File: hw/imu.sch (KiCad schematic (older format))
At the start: 1 part

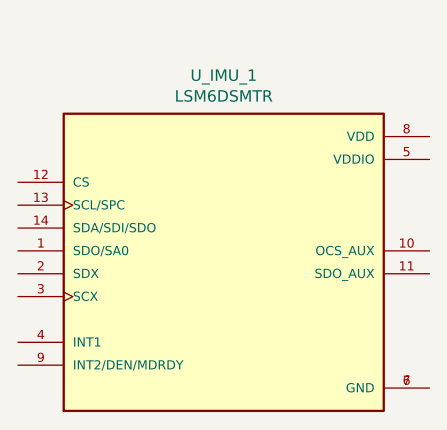
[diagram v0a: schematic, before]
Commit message: add esp32 and IMU components to schematics
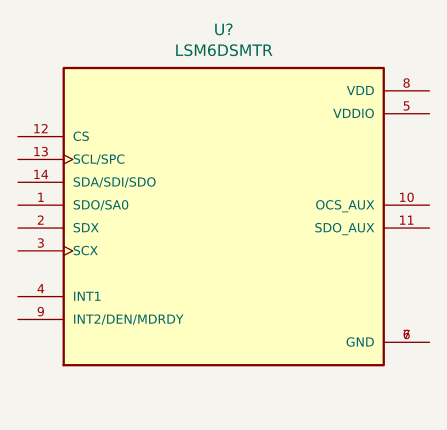
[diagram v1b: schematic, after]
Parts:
- removed U_IMU_1: LSM6DSMTR, PQFN50P300X250X86-14N, symbol LSM6DSMTR:LSM6DSMTR
- added U?: LSM6DSMTR, PQFN50P300X250X86-14N, symbol LSM6DSMTR:LSM6DSMTR
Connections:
- new net: U?.6 (GND), U?.7 (GND)
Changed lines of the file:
@@
 $EndDescr
 $Comp
-L LSM6DSMTR:LSM6DSMTR U_IMU_1
-U 1 1 609A00F1
-P 5550 3600
-F 0 "U_IMU_1" H 5550 4367 50  0000 C CNN
-F 1 "LSM6DSMTR" H 5550 4276 50  0000 C CNN
-F 2 "PQFN50P300X250X86-14N" H 5550 3600 50  0001 L BNN
-F 3 "" H 5550 3600 50  0001 L BNN
-F 4 "Rev 7" H 5550 3600 50  0001 L BNN "PARTREV"
-F 5 "STMicroelectronics" H 5550 3600 50  0001 L BNN "MANUFACTURER"
-F 6 "0.86 mm" H 5550 3600 50  0001 L BNN "MAXIMUM_PACKAGE_HEIGHT"
-F 7 "IPC 7351B" H 5550 3600 50  0001 L BNN "STANDARD"
-	1    5550 3600
+L LSM6DSMTR:LSM6DSMTR U?
+U 1 1 609A2074
+P 5550 3400
+F 0 "U?" H 5550 4167 50  0000 C CNN
+F 1 "LSM6DSMTR" H 5550 4076 50  0000 C CNN
+F 2 "PQFN50P300X250X86-14N" H 5550 3400 50  0001 L BNN
+F 3 "" H 5550 3400 50  0001 L BNN
+F 4 "Rev 7" H 5550 3400 50  0001 L BNN "PARTREV"
+F 5 "STMicroelectronics" H 5550 3400 50  0001 L BNN "MANUFACTURER"
+F 6 "0.86 mm" H 5550 3400 50  0001 L BNN "MAXIMUM_PACKAGE_HEIGHT"
+F 7 "IPC 7351B" H 5550 3400 50  0001 L BNN "STANDARD"
+	1    5550 3400
 	1    0    0    -1
 $EndComp

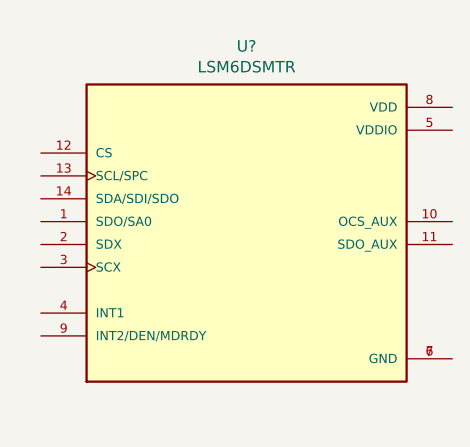
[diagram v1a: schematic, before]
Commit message: Modified ESP32 and IMU symbol properties. Generated netlist and tables as example
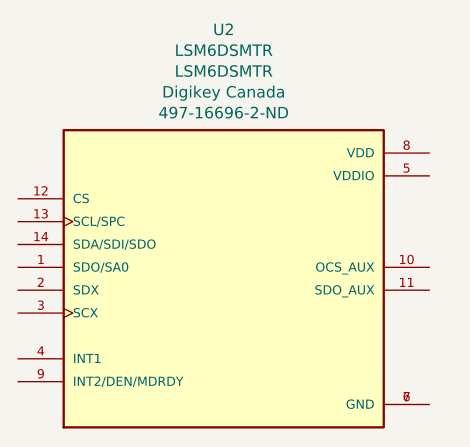
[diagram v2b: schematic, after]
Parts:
- removed U?: LSM6DSMTR, PQFN50P300X250X86-14N, symbol LSM6DSMTR:LSM6DSMTR
- added U2: LSM6DSMTR, footprints:LSM6DSMTR, symbol LSM6DSMTR:LSM6DSMTR
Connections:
- new net: U2.6 (GND), U2.7 (GND)
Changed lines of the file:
@@
 $EndDescr
 $Comp
-L LSM6DSMTR:LSM6DSMTR U?
-U 1 1 609A2074
-P 5550 3400
-F 0 "U?" H 5550 4167 50  0000 C CNN
-F 1 "LSM6DSMTR" H 5550 4076 50  0000 C CNN
-F 2 "PQFN50P300X250X86-14N" H 5550 3400 50  0001 L BNN
-F 3 "" H 5550 3400 50  0001 L BNN
-F 4 "Rev 7" H 5550 3400 50  0001 L BNN "PARTREV"
-F 5 "STMicroelectronics" H 5550 3400 50  0001 L BNN "MANUFACTURER"
-F 6 "0.86 mm" H 5550 3400 50  0001 L BNN "MAXIMUM_PACKAGE_HEIGHT"
-F 7 "IPC 7351B" H 5550 3400 50  0001 L BNN "STANDARD"
-	1    5550 3400
+L LSM6DSMTR:LSM6DSMTR U2
+U 1 1 609A33A3
+P 5450 3600
+F 0 "U2" H 5450 4639 50  0000 C CNN
+F 1 "LSM6DSMTR" H 5450 4548 50  0000 C CNN
+F 2 "footprints:LSM6DSMTR" H 5450 3600 50  0001 L BNN
+F 3 "http://www.st.com/content/ccc/resource/technical/document/datasheet/76/27/cf/88/c5/03/42/6b/DM00218116.pdf/files/DM00218116.pdf/jcr:content/translations/en.DM00218116.pdf" H 5450 3600 50  0001 L BNN
+F 4 "Rev 7" H 5450 3600 50  0001 L BNN "PARTREV"
+F 5 "0.86 mm" H 5450 3600 50  0001 L BNN "MAXIMUM_PACKAGE_HEIGHT"
+F 6 "IPC 7351B" H 5450 3600 50  0001 L BNN "STANDARD"
+F 7 "STMicroelectronics" H 5450 3600 50  0001 L BNN "Manufacturer"
+F 8 "LSM6DSMTR" H 5450 4457 50  0000 C CNN "Manufacturer Product Number"
+F 9 "Digikey Canada" H 5450 4366 50  0000 C CNN "Vendor"
+F 10 "497-16696-2-ND" H 5450 4275 50  0000 C CNN "Vendor Product Number"
+	1    5450 3600
 	1    0    0    -1
 $EndComp

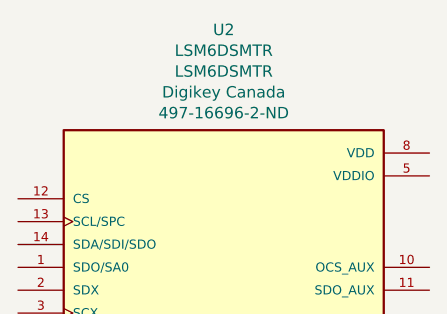
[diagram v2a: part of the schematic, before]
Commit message: Updated schematics and footprints to use default shared libraries. Updated general schematic
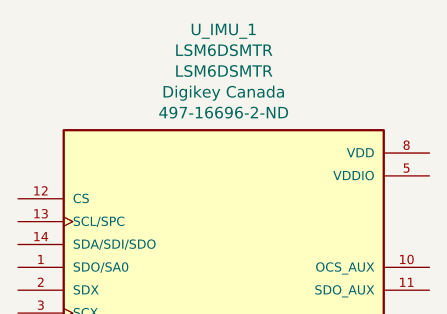
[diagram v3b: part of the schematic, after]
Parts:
- U_IMU_1: renamed from U2; MAXIMUM_PACKAGE_HEIGHT 0.86 mm -> (none); PARTREV Rev 7 -> (none); STANDARD IPC 7351B -> (none)
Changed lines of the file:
@@
 $EndDescr
 $Comp
-L LSM6DSMTR:LSM6DSMTR U2
+L LSM6DSMTR:LSM6DSMTR U_IMU_1
 U 1 1 609A33A3
 P 5450 3600
-F 0 "U2" H 5450 4639 50  0000 C CNN
+F 0 "U_IMU_1" H 5450 4639 50  0000 C CNN
 F 1 "LSM6DSMTR" H 5450 4548 50  0000 C CNN
 F 2 "footprints:LSM6DSMTR" H 5450 3600 50  0001 L BNN
 F 3 "http://www.st.com/content/ccc/resource/technical/document/datasheet/76/27/cf/88/c5/03/42/6b/DM00218116.pdf/files/DM00218116.pdf/jcr:content/translations/en.DM00218116.pdf" H 5450 3600 50  0001 L BNN
-F 4 "Rev 7" H 5450 3600 50  0001 L BNN "PARTREV"
-F 5 "0.86 mm" H 5450 3600 50  0001 L BNN "MAXIMUM_PACKAGE_HEIGHT"
-F 6 "IPC 7351B" H 5450 3600 50  0001 L BNN "STANDARD"
-F 7 "STMicroelectronics" H 5450 3600 50  0001 L BNN "Manufacturer"
-F 8 "LSM6DSMTR" H 5450 4457 50  0000 C CNN "Manufacturer Product Number"
-F 9 "Digikey Canada" H 5450 4366 50  0000 C CNN "Vendor"
-F 10 "497-16696-2-ND" H 5450 4275 50  0000 C CNN "Vendor Product Number"
+F 4 "STMicroelectronics" H 5450 3600 50  0001 L BNN "Manufacturer"
+F 5 "LSM6DSMTR" H 5450 4457 50  0000 C CNN "Manufacturer Product Number"
+F 6 "Digikey Canada" H 5450 4366 50  0000 C CNN "Vendor"
+F 7 "497-16696-2-ND" H 5450 4275 50  0000 C CNN "Vendor Product Number"
 	1    5450 3600
 	1    0    0    -1

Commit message: minor changes
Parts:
- added IMU_C1: 0.1uF, footprints:C1206S104K5RACAUTO, symbol Device:C_Small
- added IMU_R1, IMU_R2: 4.7k, footprints:RESC1508X55N, symbol Device:R
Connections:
- net labels added: +3.3V, +3.3V_cap, GND, IMU_INT1, IMU_INT2, IMU_SCL, IMU_SDA, IMU_SDO_SA0
- wire segments 0 -> 28
- no-connect marks 0 -> 2
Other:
- moved on the sheet: U_IMU_1
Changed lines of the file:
@@
 $EndDescr
+$Comp
+L power:+3.3V #PWR?
+U 1 1 60AD089D
+P 1550 1200
+F 0 "#PWR?" H 1550 1050 50  0001 C CNN
+F 1 "+3.3V" H 1565 1373 50  0000 C CNN
+F 2 "" H 1550 1200 50  0001 C CNN
+F 3 "" H 1550 1200 50  0001 C CNN
+	1    1550 1200
+	1    0    0    -1
+$EndComp
+$Comp
+L power:+3.3V #PWR?
+U 1 1 60ACF823
+P 3450 2400
+F 0 "#PWR?" H 3450 2250 50  0001 C CNN
+F 1 "+3.3V" H 3465 2573 50  0000 C CNN
+F 2 "" H 3450 2400 50  0001 C CNN
+F 3 "" H 3450 2400 50  0001 C CNN
+	1    3450 2400
+	1    0    0    -1
+$EndComp
+Wire Wire Line
+	4150 3700 4150 4200
+$Comp
+L power:GND #PWR?
+U 1 1 60ACE4E5
+P 6600 4350
+F 0 "#PWR?" H 6600 4100 50  0001 C CNN
+F 1 "GND" H 6605 4177 50  0000 C CNN
+F 2 "" H 6600 4350 50  0001 C CNN
+F 3 "" H 6600 4350 50  0001 C CNN
+	1    6600 4350
+	1    0    0    -1
+$EndComp
+$Comp
+L power:GND #PWR?
+U 1 1 60ACD629
+P 4150 4200
+F 0 "#PWR?" H 4150 3950 50  0001 C CNN
+F 1 "GND" H 4155 4027 50  0000 C CNN
+F 2 "" H 4150 4200 50  0001 C CNN
+F 3 "" H 4150 4200 50  0001 C CNN
+	1    4150 4200
+	1    0    0    -1
+$EndComp
+$Comp
+L power:GND #PWR?
+U 1 1 60ACC949
+P 1550 2000
+F 0 "#PWR?" H 1550 1750 50  0001 C CNN
+F 1 "GND" H 1555 1827 50  0000 C CNN
+F 2 "" H 1550 2000 50  0001 C CNN
+F 3 "" H 1550 2000 50  0001 C CNN
+	1    1550 2000
+	1    0    0    -1
+$EndComp
+Wire Wire Line
+	1550 1750 1550 2000
+Connection ~ 3450 2700
+Wire Wire Line
+	3450 2400 3450 2700
+Wire Wire Line
+	3450 2700 3450 2800
+Wire Wire Line
+	3950 2700 3450 2700
+Wire Wire Line
+	3950 2800 3950 2700
+Wire Wire Line
+	2400 3300 3950 3300
+Wire Wire Line
+	3950 3300 4650 3300
+Connection ~ 3950 3300
+Wire Wire Line
+	4200 3200 4650 3200
+Text Label 4200 3200 0    50   ~ 0
++3.3V_cap
+$Comp
+L Device:R IMU_R2
+U 1 1 60A2D06B
+P 3950 2950
+F 0 "IMU_R2" H 4020 2996 50  0000 L CNN
+F 1 "4.7k" H 4020 2905 50  0000 L CNN
+F 2 "footprints:RESC1508X55N" V 3880 2950 50  0001 C CNN
+F 3 "~https://www.vishay.com/docs/28760/mcat_pro.pdf" H 3950 2950 50  0001 C CNN
+F 4 "Digikey" H 3950 2950 50  0001 C CNN "Vendor"
+F 5 "MCT0603-4.7K-MDCT-ND" H 3950 2950 50  0001 C CNN "Vendor Part Number"
+F 6 "Vishay Beyschlag/Draloric/BC Components" H 3950 2950 50  0001 C CNN "Manufacturer"
+F 7 "MCT0603MD4701DP500" H 3950 2950 50  0001 C CNN "Manufacturer Part Number"
+	1    3950 2950
+	1    0    0    -1
+$EndComp
+Wire Wire Line
+	6600 4100 6600 4350
+Wire Wire Line
+	6450 4100 6600 4100
+Wire Wire Line
+	3950 3100 3950 3300
+Wire Wire Line
+	3450 3400 4650 3400
+Connection ~ 3450 3400
+Wire Wire Line
+	3450 3100 3450 3400
+$Comp
+L Device:R IMU_R1
+U 1 1 60A29787
+P 3450 2950
+F 0 "IMU_R1" H 3520 2996 50  0000 L CNN
+F 1 "4.7k" H 3520 2905 50  0000 L CNN
+F 2 "footprints:RESC1508X55N" V 3380 2950 50  0001 C CNN
+F 3 "~https://www.vishay.com/docs/28760/mcat_pro.pdf" H 3450 2950 50  0001 C CNN
+F 4 "Digikey" H 3450 2950 50  0001 C CNN "Vendor"
+F 5 "MCT0603-4.7K-MDCT-ND" H 3450 2950 50  0001 C CNN "Vendor Part Number"
+F 6 "Vishay Beyschlag/Draloric/BC Components" H 3450 2950 50  0001 C CNN "Manufacturer"
+F 7 "MCT0603MD4701DP500" H 3450 2950 50  0001 C CNN "Manufacturer Part Number"
+	1    3450 2950
+	1    0    0    -1
+$EndComp
+Connection ~ 4150 3700
+Wire Wire Line
+	4650 3700 4150 3700
+Wire Wire Line
+	4150 3600 4150 3700
+Wire Wire Line
+	4650 3600 4150 3600
+Wire Wire Line
+	6600 3000 6600 3100
+Connection ~ 6600 3000
+Wire Wire Line
+	6450 3000 6600 3000
+Wire Wire Line
+	6600 3100 6450 3100
+Wire Wire Line
+	6600 2750 6600 3000
+Text Label 6600 2750 0    50   ~ 0
++3.3V_cap
+Wire Wire Line
+	1550 1400 1550 1550
+Connection ~ 1550 1400
+Wire Wire Line
+	2000 1400 1550 1400
+Text Label 2000 1400 0    50   ~ 0
++3.3V_cap
+Wire Wire Line
+	1550 1200 1550 1400
+$Comp
+L Device:C_Small IMU_C1
+U 1 1 60A1BC4F
+P 1550 1650
+F 0 "IMU_C1" H 1642 1696 50  0000 L CNN
+F 1 "0.1uF" H 1642 1605 50  0000 L CNN
+F 2 "footprints:C1206S104K5RACAUTO" H 1550 1650 50  0001 C CNN
+F 3 "~https://content.kemet.com/datasheets/KEM_C1014_X7R_FE-CAP_SMD.pdf" H 1550 1650 50  0001 C CNN
+F 4 "Digikey" H 1550 1650 50  0001 C CNN "Vendor"
+F 5 "399-C1206S104K5RACAUTOCT-ND" H 1550 1650 50  0001 C CNN "Vendor Part Number"
+F 6 "KEMET" H 1550 1650 50  0001 C CNN "Manufacturer"
+F 7 "C1206S104K5RACAUTO" H 1550 1650 50  0001 C CNN "Manufacturer Part Number"
+	1    1550 1650
+	1    0    0    -1
+$EndComp
+NoConn ~ 6450 3600
+NoConn ~ 6450 3500
+Wire Wire Line
+	2400 4000 4650 4000
+Wire Wire Line
+	2400 3900 4650 3900
+Wire Wire Line
+	2400 3500 4650 3500
+Wire Wire Line
+	2400 3400 3450 3400
+Text HLabel 2400 3400 0    50   Output ~ 0
+IMU_SDA
+Text HLabel 2400 3900 0    50   Input ~ 0
+IMU_INT1
+Text HLabel 2400 3500 0    50   Output ~ 0
+IMU_SDO_SA0
+Text HLabel 2400 3300 0    50   Input ~ 0
+IMU_SCL
 $Comp
 L LSM6DSMTR:LSM6DSMTR U_IMU_1
 U 1 1 609A33A3
-P 5450 3600
-F 0 "U_IMU_1" H 5450 4639 50  0000 C CNN
-F 1 "LSM6DSMTR" H 5450 4548 50  0000 C CNN
-F 2 "footprints:LSM6DSMTR" H 5450 3600 50  0001 L BNN
-F 3 "http://www.st.com/content/ccc/resource/technical/document/datasheet/76/27/cf/88/c5/03/42/6b/DM00218116.pdf/files/DM00218116.pdf/jcr:content/translations/en.DM00218116.pdf" H 5450 3600 50  0001 L BNN
-F 4 "STMicroelectronics" H 5450 3600 50  0001 L BNN "Manufacturer"
-F 5 "LSM6DSMTR" H 5450 4457 50  0000 C CNN "Manufacturer Product Number"
-F 6 "Digikey Canada" H 5450 4366 50  0000 C CNN "Vendor"
-F 7 "497-16696-2-ND" H 5450 4275 50  0000 C CNN "Vendor Product Number"
-	1    5450 3600
+P 5550 3500
+F 0 "U_IMU_1" H 5550 4539 50  0000 C CNN
+F 1 "LSM6DSMTR" H 5550 4448 50  0000 C CNN
+F 2 "footprints:LSM6DSMTR" H 5550 3500 50  0001 L BNN
+F 3 "http://www.st.com/content/ccc/resource/technical/document/datasheet/76/27/cf/88/c5/03/42/6b/DM00218116.pdf/files/DM00218116.pdf/jcr:content/translations/en.DM00218116.pdf" H 5550 3500 50  0001 L BNN
+F 4 "STMicroelectronics" H 5550 3500 50  0001 L BNN "Manufacturer"
+F 5 "LSM6DSMTR" H 5550 4357 50  0000 C CNN "Manufacturer Product Number"
+F 6 "Digikey Canada" H 5550 4266 50  0000 C CNN "Vendor"
+F 7 "497-16696-2-ND" H 5550 4175 50  0000 C CNN "Vendor Product Number"
+	1    5550 3500
 	1    0    0    -1
 $EndComp
+Text HLabel 2400 4000 0    50   Input ~ 0
+IMU_INT2
 $EndSCHEMATC

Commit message: Combining the ESP and IMU Modules
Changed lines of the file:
@@
 $Descr USLetter 11000 8500
 encoding utf-8
-Sheet 3 3
+Sheet 4 4
 Title "IMU | Rover Controller"
 Date "2021-05-10"
@@
 Wire Wire Line
 	2400 3400 3450 3400
-Text HLabel 2400 3400 0    50   Output ~ 0
-IMU_SDA
 Text HLabel 2400 3900 0    50   Input ~ 0
 IMU_INT1
-Text HLabel 2400 3500 0    50   Output ~ 0
-IMU_SDO_SA0
 Text HLabel 2400 3300 0    50   Input ~ 0
 IMU_SCL
@@
 Text HLabel 2400 4000 0    50   Input ~ 0
 IMU_INT2
+Text HLabel 2400 3400 0    50   BiDi ~ 0
+IMU_SDA
+Text HLabel 2400 3500 0    50   Input ~ 0
+IMU_SDO_SA0
 $EndSCHEMATC
